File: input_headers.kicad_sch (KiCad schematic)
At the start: 3 parts, among them J2 171856-0002, J6 171856-0002, J9 TLW-104-05-T-D

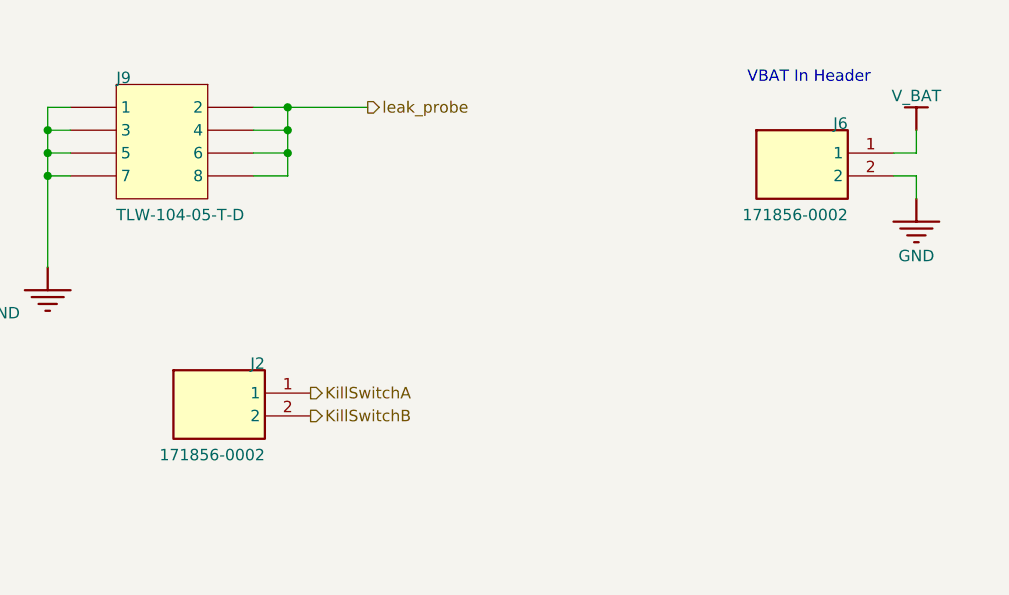
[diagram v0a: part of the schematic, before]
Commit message: Finished updating all input and output headers
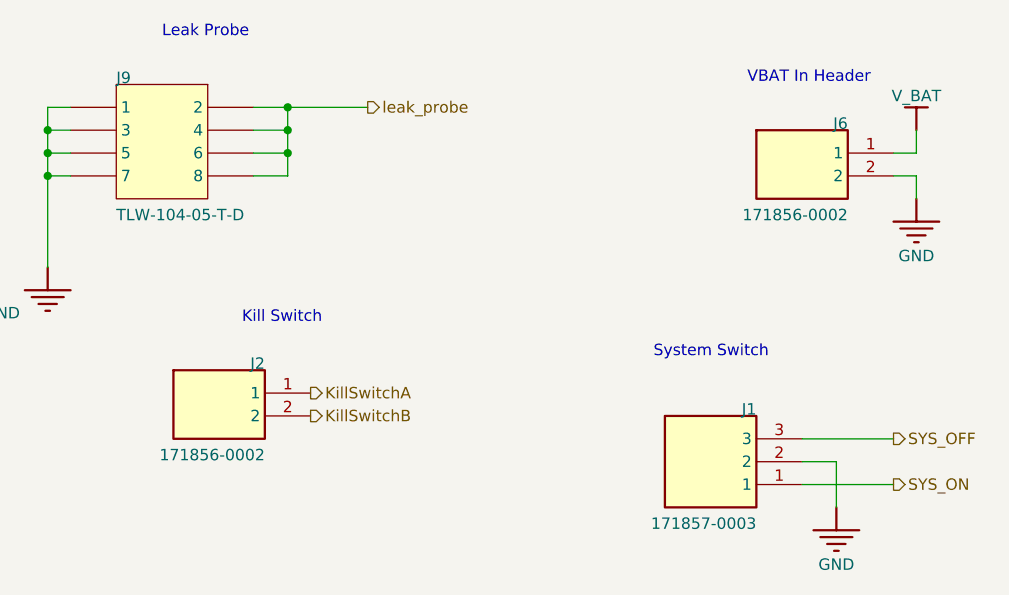
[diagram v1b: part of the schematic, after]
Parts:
- added J1: 171857-0003, AltiumImport:171857-0003, symbol MEB-altium-import:system_SSR_control_0_171857-0003
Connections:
- net GND: now also J1.2
- new net SYS_OFF: J1.3
- new net SYS_ON: J1.1
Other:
- note added: "Kill Switch"
- note added: "Leak Probe"
- note added: "System Switch"
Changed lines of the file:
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@@
   (junction (at 11.43 30.48) (diameter 0) (color 0 0 0 0)
   )
+  (wire (pts (xy 99.06 72.39) (xy 99.06 67.31))
+    (stroke (width 0) (type default))
+  )
   (wire (pts (xy 107.95 33.02) (xy 107.95 30.48))
     (stroke (width 0.254) (type default))
@@
     (stroke (width 0.254) (type default))
   )
+  (wire (pts (xy 99.06 67.31) (xy 95.25 67.31))
+    (stroke (width 0) (type default))
+  )
   (wire (pts (xy 38.1 33.02) (xy 34.29 33.02))
     (stroke (width 0) (type default))
@@
     (stroke (width 0) (type default))
   )
+  (wire (pts (xy 95.25 64.77) (xy 105.41 64.77))
+    (stroke (width 0) (type default))
+  )
   (wire (pts (xy 11.43 35.56) (xy 13.97 35.56))
     (stroke (width 0) (type default))
@@
   )
   (wire (pts (xy 38.1 27.94) (xy 34.29 27.94))
+    (stroke (width 0) (type default))
+  )
+  (wire (pts (xy 95.25 69.85) (xy 105.41 69.85))
     (stroke (width 0) (type default))
   )
@@
     (effects (font (size 1.27 1.27)) (justify right bottom))
   )
+  (text "Kill Switch" (at 33.02 52.07 0)
+    (effects (font (size 1.27 1.27)) (justify left bottom))
+  )
+  (text "Leak Probe" (at 24.13 20.32 0)
+    (effects (font (size 1.27 1.27)) (justify left bottom))
+  )
+  (text "System Switch" (at 78.74 55.88 0)
+    (effects (font (size 1.27 1.27)) (justify left bottom))
+  )
+  (hierarchical_label "SYS_ON" (shape output) (at 105.41 69.85 0) (fields_autoplaced)
+    (effects (font (size 1.27 1.27)) (justify left))
+  )
   (hierarchical_label "KillSwitchB" (shape output) (at 40.64 62.23 0) (fields_autoplaced)
     (effects (font (size 1.27 1.27)) (justify left))
@@
     (effects (font (size 1.27 1.27)) (justify left))
   )
+  (hierarchical_label "SYS_OFF" (shape output) (at 105.41 64.77 0) (fields_autoplaced)
+    (effects (font (size 1.27 1.27)) (justify left))
+  )
   (hierarchical_label "KillSwitchA" (shape output) (at 40.64 59.69 0) (fields_autoplaced)
     (effects (font (size 1.27 1.27)) (justify left))
+  )
+  (symbol (lib_id "MEB-altium-import:GND") (at 99.06 72.39 0) (mirror y) (unit 1)
+    (in_bom yes) (on_board yes) (dnp no)
+    (property "Reference" "#PWR0127" (at 99.06 72.39 0)
+      (effects (font (size 1.27 1.27)) hide)
+    )
+    (property "Value" "GND" (at 99.06 78.74 0)
+      (effects (font (size 1.27 1.27)))
+    )
+    (property "Footprint" "" (at 99.06 72.39 0)
+      (effects (font (size 1.27 1.27)) hide)
+    )
+    (property "Datasheet" "" (at 99.06 72.39 0)
+      (effects (font (size 1.27 1.27)) hide)
+    )
+    (pin "")
+    (instances
+      (project "MEB"
+        (path "/228e4997-23c1-4c21-939b-583cad26a5e3/90a8e139-216e-4b02-83ea-4edb1f5f4c15"
+          (reference "#PWR0127") (unit 1)
+        )
+        (path "/228e4997-23c1-4c21-939b-583cad26a5e3/3aab6a70-cc66-4393-a750-92acad576aaa"
+          (reference "#PWR04") (unit 1)
+        )
+      )
+    )
   )
   (symbol (lib_id "MEB-altium-import:leak_sensor_0_Header 4X2") (at 19.05 25.4 0) (unit 1)
@@
         )
       )
+    )
+  )
+  (symbol (lib_id "MEB-altium-import:system_SSR_control_0_171857-0003") (at 95.25 64.77 0) (mirror y) (unit 1)
+    (in_bom yes) (on_board yes) (dnp no)
+    (property "Reference" "J1" (at 90.17 62.23 0)
+      (effects (font (size 1.27 1.27)) (justify left bottom))
+    )
+    (property "Value" "171857-0003" (at 90.17 74.93 0)
+      (effects (font (size 1.27 1.27)) (justify left bottom))
+    )
+    (property "Footprint" "AltiumImport:171857-0003" (at 95.25 64.77 0)
+      (effects (font (size 1.27 1.27)) hide)
+    )
+    (property "Datasheet" "" (at 95.25 64.77 0)
+      (effects (font (size 1.27 1.27)) hide)
+    )
+    (property "Part Number" "171857-0003" (at 95.25 64.77 0)
+      (effects (font (size 1.27 1.27)) hide)
+    )
+    (pin "1")
+    (pin "2")
+    (pin "3")
+    (instances
+      (project "MEB"
+        (path "/228e4997-23c1-4c21-939b-583cad26a5e3/d2748488-1aa2-4890-bfa9-60c09f864312"
+          (reference "J1") (unit 1)
+        )
+        (path "/228e4997-23c1-4c21-939b-583cad26a5e3/3aab6a70-cc66-4393-a750-92acad576aaa"
+          (reference "J1") (unit 1)
+        )
+      )

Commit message: Started Working on MCU Interface
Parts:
- added J7: Conn_01x07, symbol Connector_Generic:Conn_01x07
- added R8: 0, symbol Device:R_US
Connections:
- net GND: now also J7.1 (Pin_1)
- new net: J7.3 (Pin_3), R8.2
- new net 3V3: R8.1
- new net 5V: J7.2 (Pin_2)
- new net SBW_TCK: J7.7 (Pin_7)
- new net SBW_TDIO: J7.6 (Pin_6)
- new net dbgRXD: J7.4 (Pin_4)
- new net dbgTXD: J7.5 (Pin_5)

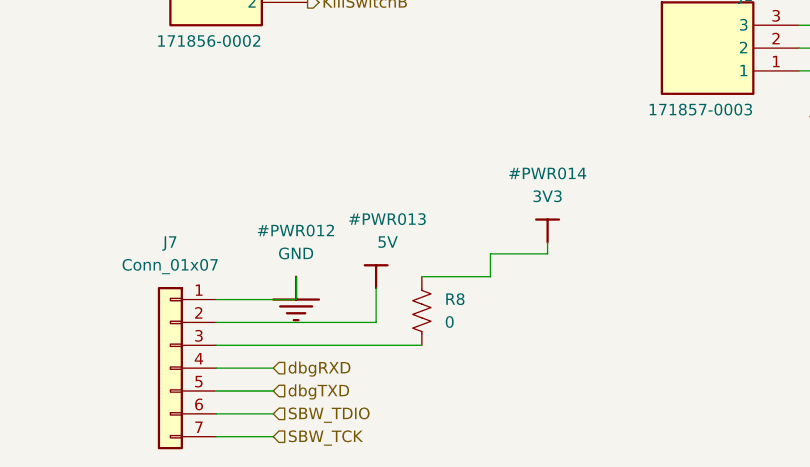
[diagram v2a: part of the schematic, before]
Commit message: Updated Ports and Components in MCU Interface
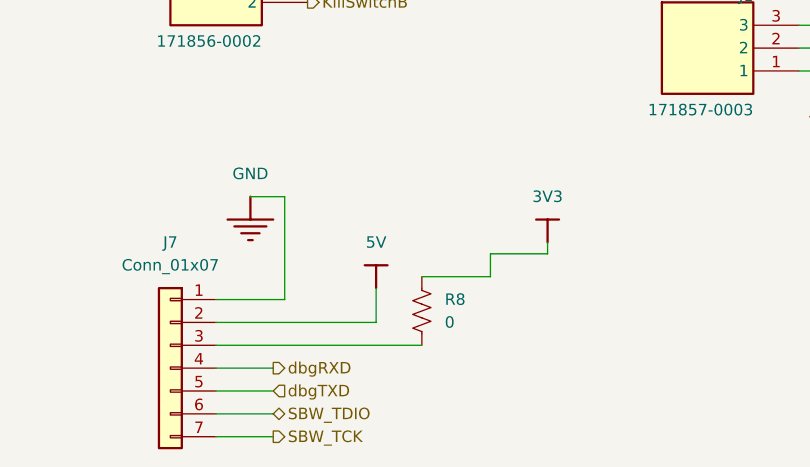
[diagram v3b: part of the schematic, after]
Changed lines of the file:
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@@
+    (stroke (width 0) (type default))
+  )
+  (wire (pts (xy 38.1 83.82) (xy 34.29 83.82))
     (stroke (width 0) (type default))
   )
@@
     (stroke (width 0) (type default))
   )
-  (wire (pts (xy 39.37 92.71) (xy 39.37 95.25))
-    (stroke (width 0) (type default))
-  )
   (wire (pts (xy 38.1 35.56) (xy 38.1 33.02))
+    (stroke (width 0) (type default))
+  )
+  (wire (pts (xy 38.1 95.25) (xy 38.1 83.82))
     (stroke (width 0) (type default))
   )
@@
     (stroke (width 0) (type default))
   )
-  (wire (pts (xy 30.48 95.25) (xy 39.37 95.25))
+  (wire (pts (xy 30.48 95.25) (xy 38.1 95.25))
     (stroke (width 0) (type default))
   )
@@
     (effects (font (size 1.27 1.27)) (justify left bottom))
   )
-  (hierarchical_label "SBW_TCK" (shape input) (at 36.83 110.49 0) (fields_autoplaced)
+  (hierarchical_label "SBW_TCK" (shape output) (at 36.83 110.49 0) (fields_autoplaced)
     (effects (font (size 1.27 1.27)) (justify left))
   )
@@
     (effects (font (size 1.27 1.27)) (justify left))
   )
-  (hierarchical_label "SBW_TDIO" (shape input) (at 36.83 107.95 0) (fields_autoplaced)
+  (hierarchical_label "SBW_TDIO" (shape bidirectional) (at 36.83 107.95 0) (fields_autoplaced)
     (effects (font (size 1.27 1.27)) (justify left))
   )
@@
     (effects (font (size 1.27 1.27)) (justify left))
   )
-  (hierarchical_label "dbgRXD" (shape input) (at 36.83 102.87 0) (fields_autoplaced)
+  (hierarchical_label "dbgRXD" (shape output) (at 36.83 102.87 0) (fields_autoplaced)
     (effects (font (size 1.27 1.27)) (justify left))
   )
@@
     (effects (font (size 1.27 1.27)) (justify left))
   )
-  (symbol (lib_id "MEB-altium-import:GND") (at 39.37 92.71 0) (unit 1)
-    (in_bom yes) (on_board yes) (dnp no)
-    (property "Reference" "#PWR012" (at 39.37 87.63 0)
+  (symbol (lib_id "MEB-altium-import:GND") (at 34.29 83.82 0) (unit 1)
+    (in_bom yes) (on_board yes) (dnp no)
+    (property "Reference" "#PWR012" (at 34.29 78.74 0)
+      (effects (font (size 1.27 1.27)) hide)
+    )
+    (property "Value" "GND" (at 34.29 81.28 0)
       (effects (font (size 1.27 1.27)))
     )
-    (property "Value" "GND" (at 39.37 90.17 0)
-      (effects (font (size 1.27 1.27)))
-    )
-    (property "Footprint" "" (at 39.37 92.71 0)
-      (effects (font (size 1.27 1.27)) hide)
-    )
-    (property "Datasheet" "" (at 39.37 92.71 0)
+    (property "Footprint" "" (at 34.29 83.82 0)
+      (effects (font (size 1.27 1.27)) hide)
+    )
+    (property "Datasheet" "" (at 34.29 83.82 0)
       (effects (font (size 1.27 1.27)) hide)
     )
@@
     (in_bom yes) (on_board yes) (dnp no)
     (property "Reference" "#PWR013" (at 49.53 86.36 0)
+      (effects (font (size 1.27 1.27)) hide)
+    )
+    (property "Value" "5V" (at 48.26 88.9 0)
       (effects (font (size 1.27 1.27)))
     )
-    (property "Value" "5V" (at 49.53 88.9 0)
-      (effects (font (size 1.27 1.27)))
-    )
     (property "Footprint" "" (at 48.26 93.98 0)
       (effects (font (size 1.27 1.27)) hide)
@@
     (in_bom yes) (on_board yes) (dnp no)
     (property "Reference" "#PWR014" (at 67.31 81.28 0)
-      (effects (font (size 1.27 1.27)))
+      (effects (font (size 1.27 1.27)) hide)
     )
     (property "Value" "3V3" (at 67.31 83.82 0)

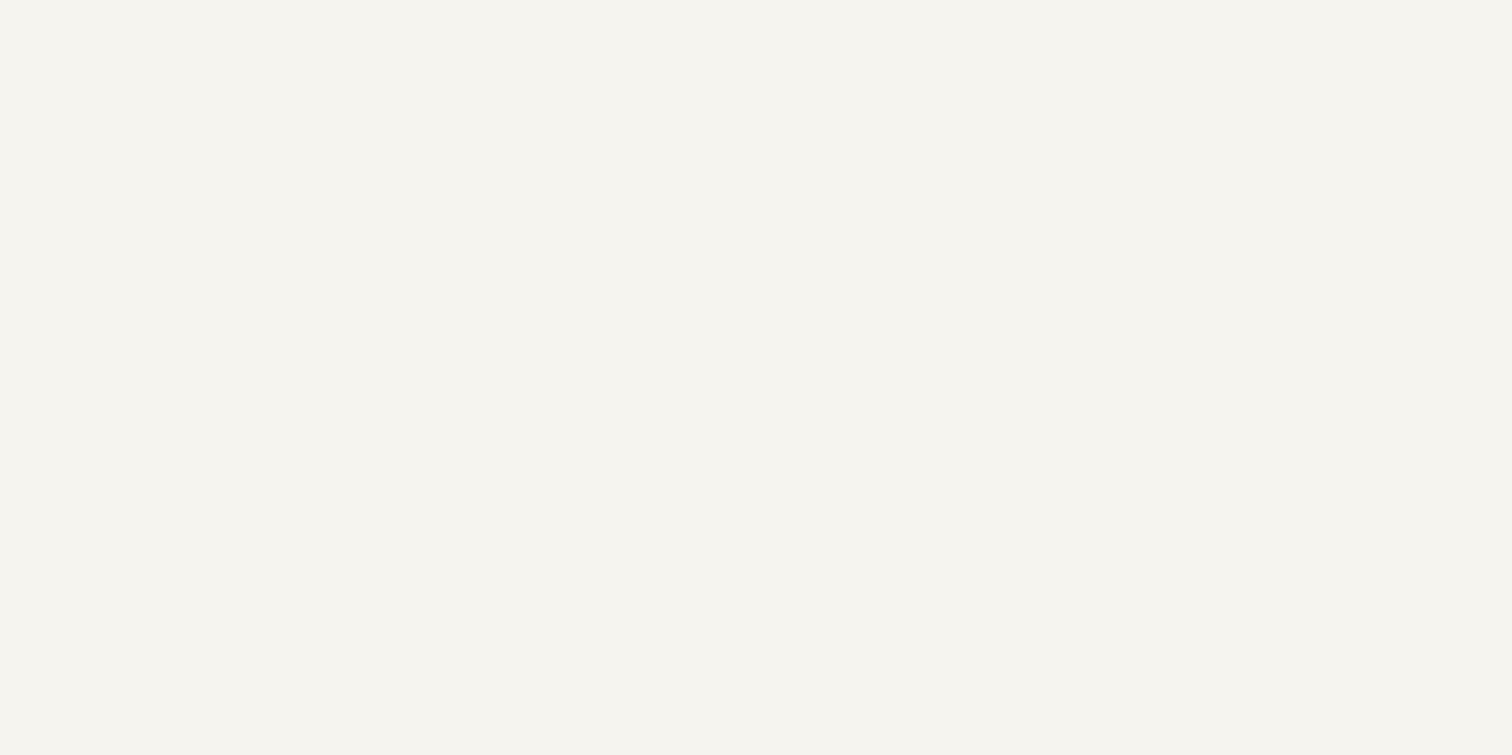
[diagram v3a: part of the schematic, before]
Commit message: added usb->uart converter chip and some components, need to finish
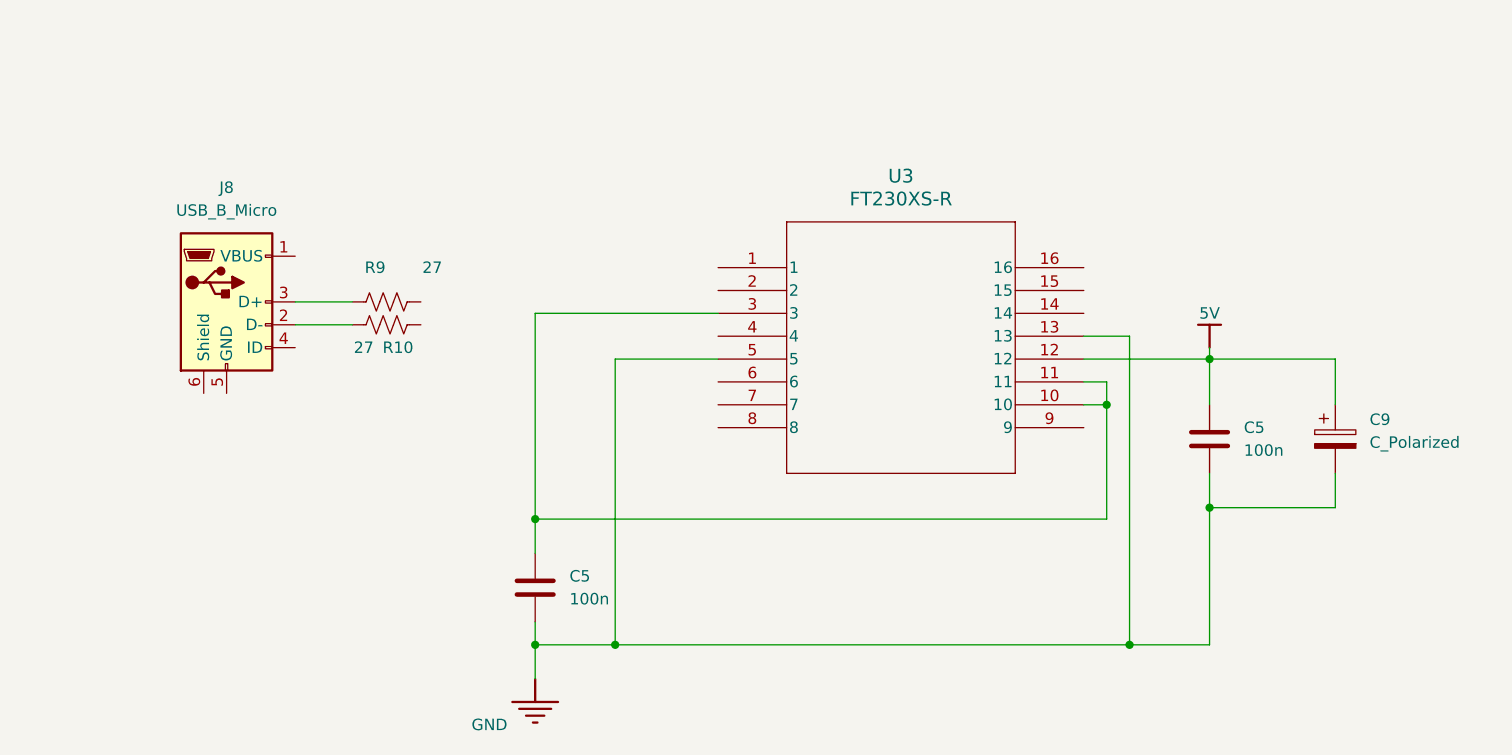
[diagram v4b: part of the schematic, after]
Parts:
- added C5 (x2): 100n, symbol Device:C
- added C9: C_Polarized, symbol Device:C_Polarized
- added J8: USB_B_Micro, symbol Connector:USB_B_Micro
- added R10, R9: 27, symbol Device:R_US
- added U3: FT230XS-R, SWLib:SOIC_30XS-R_FTD, symbol SWLib:FT230XS-R
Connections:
- net 5V: now also C5.1, C9.1, U3.12
- net GND: now also C5.2, C5.2, C9.2, U3.13, U3.5
- new net: C5.1, U3.10, U3.11, U3.3
- new net: J8.3 (D+), R9.1
- new net: J8.2 (D-), R10.1
